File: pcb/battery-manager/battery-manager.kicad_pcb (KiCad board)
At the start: 2 copper layers, 38 x 38 mm, 26 parts, among them J1 Conn_01x05_Female, J10 JST_2MM_MALE, J2 Conn_01x04_Female, J3 Conn_01x04_Female, J4 Conn_01x04_Female, J5 Conn_01x04_Female, J6 Conn_01x04_Female, J7 Conn_01x04_Female, J8 Conn_01x04_Female, J9 JST_2MM_MALE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

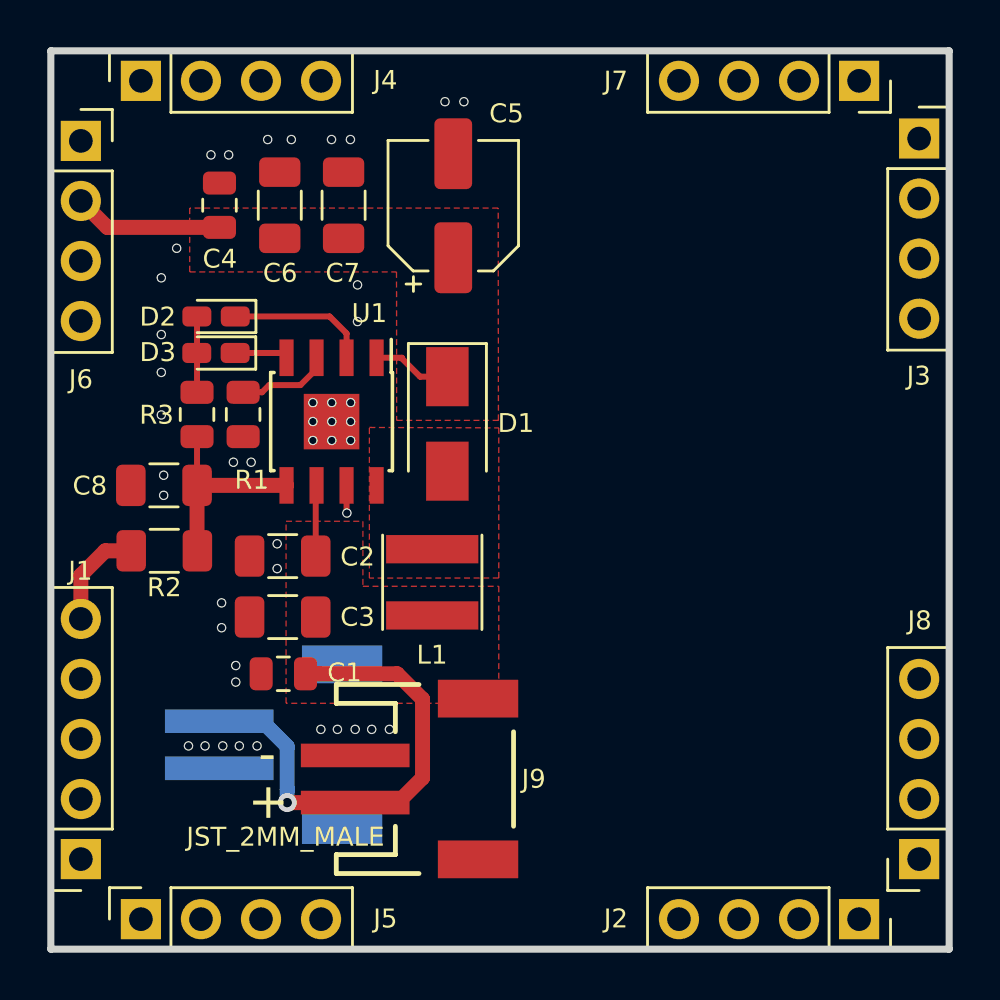
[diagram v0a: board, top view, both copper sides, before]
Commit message: pcb: update battery shield pcb to latest version
mainly, add a power path to supply the target with power when the
TP5400 is charging the battery, as in this mode the boost converter is
not active and the target is supplied with the current battery voltage
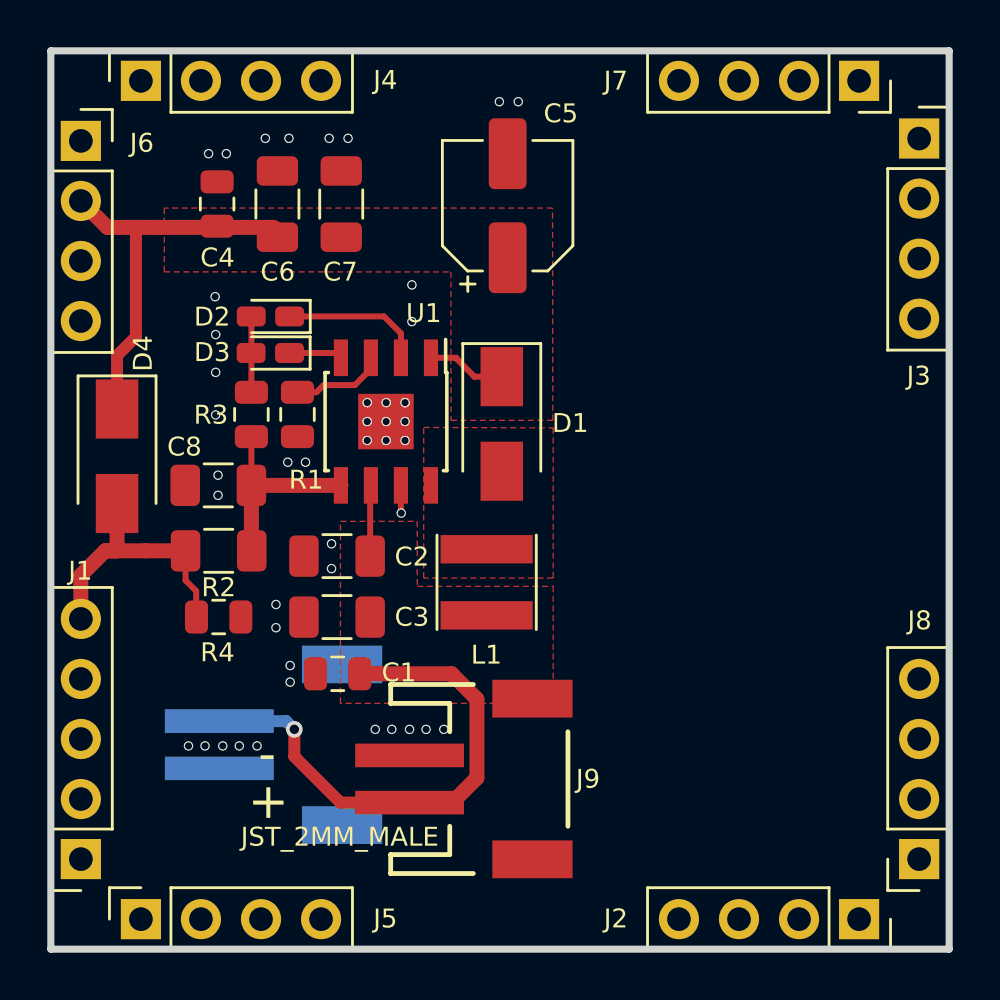
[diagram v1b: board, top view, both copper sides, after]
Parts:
- added D4: SS32, Diode_SMD:D_SMA, F.Cu at (122.8, 79.2)
- added R4: 5k, Resistor_SMD:R_0805_2012Metric, F.Cu at (127.1, 86.0)
- moved C1 2.30 mm to (132.1, 88.4)
- moved C2 2.30 mm to (132.1, 83.4)
- moved C3 2.30 mm to (132.1, 86.0)
- moved C5 2.30 mm to (139.3, 68.6)
- moved D2 2.30 mm to (129.3, 73.2)
- moved D3 2.30 mm to (129.3, 74.8)
- moved C8 2.30 mm to (127.1, 80.4)
- moved R2 2.30 mm to (127.1, 83.2)
- moved R3 2.30 mm to (128.5, 77.4)
- moved D1 2.30 mm to (139.1, 77.8)
- moved J9 2.30 mm to (138.9, 92.8)
- moved L1 2.30 mm to (138.4, 84.5)
- moved R1 2.30 mm to (130.4, 77.4)
- moved U1 2.30 mm to (134.2, 77.7)
- moved C4 0.11 mm to (127.0, 68.5)
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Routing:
- net /VOUT: track 9.67 -> 20.0 mm
- net /USB_VBUS: track 4.41 -> 12.2 mm
- net /BAT: track 23.6 -> 25.2 mm
- net GND: vias 45 -> 44
